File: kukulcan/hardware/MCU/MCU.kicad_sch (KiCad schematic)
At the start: 84 parts, among them J1 Barrel_Jack_5V_In, J2 Barrel_Jack_5V_In, J3 MiniPCIe Socket, J4 USB_C_Receptacle, J5 SMA_GNSS, Q1 AO3401A, U1 NEO-M8N, U2 ESP32-S3R16V, U3 W25Q256JWEIQ, U4 TLV1117-33, U5 BMI088, U6 BME280, U8 BNO055, X1 40MHz, Y1 32.768kHz

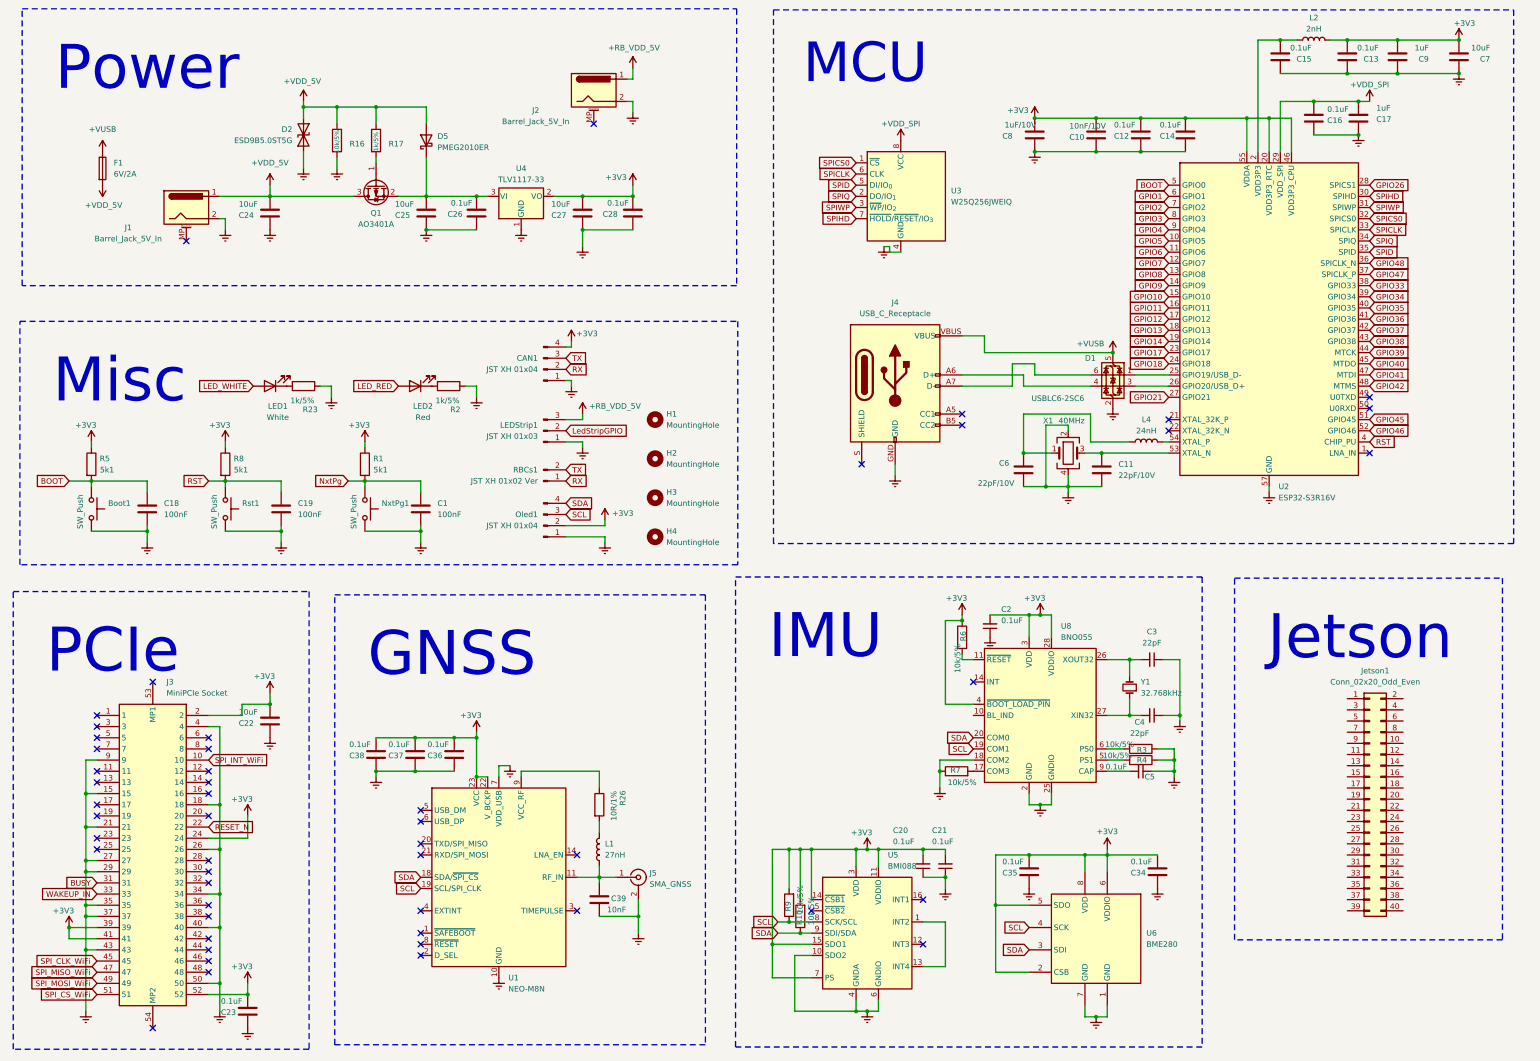
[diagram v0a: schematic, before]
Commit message: feat(kukulcan): several layout and schematic improvements, tasks pending. PCIe connector out.
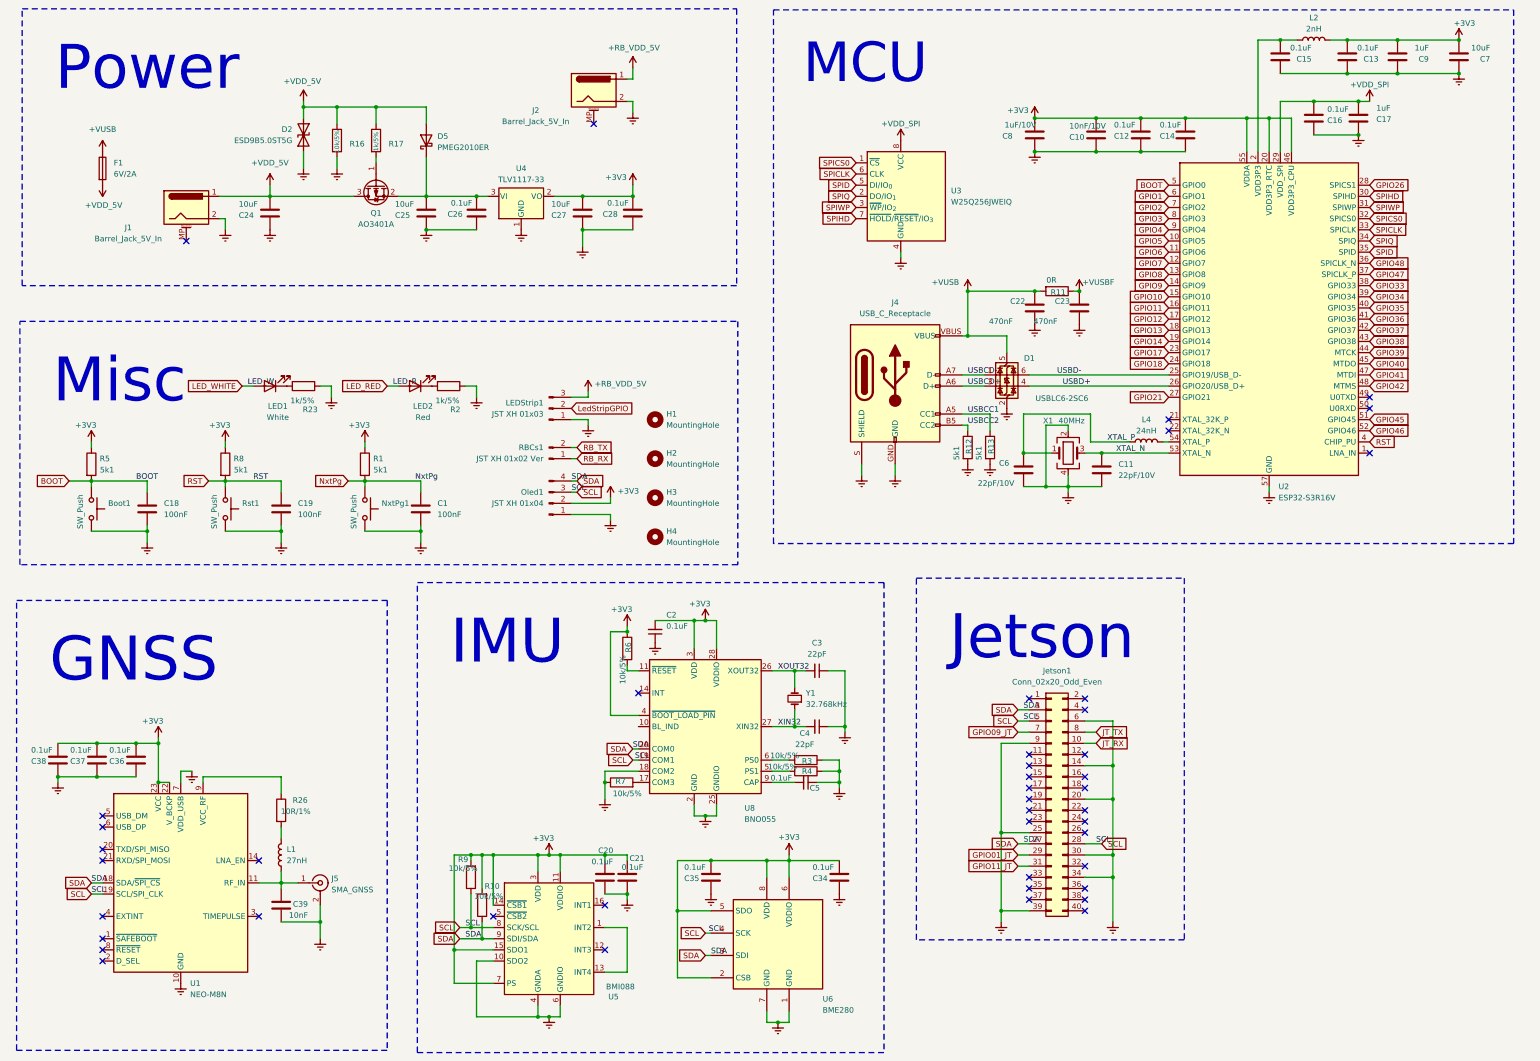
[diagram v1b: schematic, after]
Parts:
- removed C20, C21: 0.1uF, Capacitor_SMD:C_0402_1005Metric_Pad0.74x0.62mm_HandSolder, symbol PCM_SparkFun-Capacitor:C
- removed CAN1: JST XH 01x04, Connector_JST:JST_XH_S4B-XH-SM4-TB_1x04-1MP_P2.50mm_Horizontal, symbol Connector:Conn_01x04_Pin
- removed J3: MiniPCIe Socket, Core_System_2026:MiniPCIeSocket, symbol PCIeSocket:2041119-1
- added C20, C21: 0.1uF, Capacitor_SMD:C_0402_1005Metric_Pad0.74x0.62mm_HandSolder, symbol Device:C
- added R11: 0R, Resistor_SMD:R_0402_1005Metric_Pad0.72x0.64mm_HandSolder, symbol Device:R
- added R12, R13: 5k1, Resistor_SMD:R_0402_1005Metric_Pad0.72x0.64mm_HandSolder, symbol Device:R
- C22: value 10uF -> 470nF
- C23: value 0.1uF -> 470nF
- C24, C25, C27, C7: footprint Capacitor_SMD:C_0402_1005Metric_Pad0.74x0.62mm_HandSolder -> Capacitor_SMD:C_0805_2012Metric_Pad1.18x1.45mm_HandSolder
- F1: footprint Fuse:Fuse_0402_1005Metric_Pad0.77x0.64mm_HandSolder -> Fuse:Fuse_0805_2012Metric
- J4: footprint PCM_SparkFun-Connector:USB-C_16 -> Connector_USB:USB_C_Receptacle_GCT_USB4105-xx-A_16P_TopMnt_Horizontal
- LEDStrip1: footprint Connector_JST:JST_XH_S3B-XH-SM4-TB_1x03-1MP_P2.50mm_Horizontal -> Connector_JST:JST_XH_B3B-XH-A_1x03_P2.50mm_Vertical
- Oled1: footprint Connector_JST:JST_XH_S4B-XH-SM4-TB_1x04-1MP_P2.50mm_Horizontal -> Connector_JST:JST_XH_B4B-XH-A_1x04_P2.50mm_Vertical
- RBCs1: footprint Connector_JST:JST_XH_S2B-XH-A_1x02_P2.50mm_Horizontal -> Connector_JST:JST_XH_B2B-XH-A_1x02_P2.50mm_Vertical
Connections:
- net +3V3: now also C20.1, C21.1; no longer C22.1, C23.1
- net +VUSB: now also C22.2, R11.2
- net GND: now also C22.1, C23.1, J4.S (SHIELD), Jetson1.14 (Pin_14), Jetson1.20 (Pin_20), Jetson1.25 (Pin_25), Jetson1.30 (Pin_30), Jetson1.34 (Pin_34), Jetson1.39 (Pin_39), Jetson1.6 (Pin_6), Jetson1.9 (Pin_9), C20.2, C21.2, R12.2, R13.2; no longer C22.2, C23.2
- net SCL: now also Jetson1.28 (Pin_28), Jetson1.5 (Pin_5)
- net SDA: now also Jetson1.27 (Pin_27), Jetson1.3 (Pin_3)
- net USBCC1: now reaches J4.A5 (CC1)
- net USBCC1: now also R13.1
- net USBCD+: now reaches J4.A6 (D+), J4.B6 (D+)
- net USBCD+: now also D1.3 (I/O2); no longer D1.4 (I/O2)
- net USBCD-: now reaches J4.A7 (D-), J4.B7 (D-)
- net USBCD-: now also D1.1 (I/O1); no longer D1.6 (I/O1)
- net USBCC2: now reaches J4.B5 (CC2)
- net USBCC2: now also R12.1
- net USBD-: now reaches U2.25 (GPIO19/USB_D-)
- net USBD-: now also D1.6 (I/O1); no longer D1.1 (I/O1)
- net USBD+: now reaches U2.26 (GPIO20/USB_D+)
- net USBD+: now also D1.4 (I/O2); no longer D1.3 (I/O2)
- net XTAL_N: now reaches C11.1, U2.53 (XTAL_N), X1.3
- net XOUT32: now reaches C3.2, U8.26 (XOUT32), Y1.2
- net XIN32: now reaches C4.2, U8.27 (XIN32), Y1.1
- net JT_RX: now reaches Jetson1.10 (Pin_10)
- net GPIO01_JT: now reaches Jetson1.29 (Pin_29)
- net GPIO11_JT: now reaches Jetson1.31 (Pin_31)
- net GPIO09_JT: now reaches Jetson1.7 (Pin_7)
- net JT_TX: now reaches Jetson1.8 (Pin_8)
- net XTAL_P: now reaches C6.2, L4.1, X1.1
- net RX renamed RB_RX
- net TX renamed RB_TX
- new net +VUSBF: C23.2, R11.1
- no-connect marks 51 -> 44
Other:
- moved on the sheet: C2, C3, C34, C35, C36, C37, C38, C39, C4, C5, D1, J5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

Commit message: feat(kukulcan): current beta
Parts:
- removed C22, C23: 470nF, Capacitor_SMD:C_0402_1005Metric_Pad0.74x0.62mm_HandSolder, symbol Device:C
- added R12: 5k1, Resistor_SMD:R_0402_1005Metric_Pad0.72x0.64mm_HandSolder, symbol Device:R
- R11: value 0R -> 5k1
- renumbered C15 to C1, C14 to C10, C24 to C11, C25 to C12, C26 to C13, C27 to C14, C28 to C15, C6 to C16, C11 to C17, C13 to C2, C1 to C20, C2 to C21, C3 to C22, C4 to C23, C38 to C24, C37 to C25, C36 to C26, C5 to C27, C20 to C28, C21 to C29, C9 to C3, C35 to C30, C34 to C31, C39 to C32, C7 to C4, C16 to C5, C17 to C6, C8 to C7, C10 to C8, C12 to C9, D2 to D1, D5 to D2, D1 to D3, J2 to J1, J1 to J2, J4 to J3, J5 to J4, L2 to L1, L4 to L2, L1 to L3, R16 to R1, R6 to R10, R3 to R13, R4 to R14, R7 to R15, R26 to R16, R9 to R17, R10 to R18, R17 to R2, R23 to R3, R2 to R4, R12 to R5, R13 to R6, R5 to R7, R1 to R9, U4 to U1, U3 to U2, U2 to U3, U8 to U4, U1 to U5, U5 to U6, U6 to U7
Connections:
- net +VUSBF is gone; now on net +3V3: R11.1
- net GPIO33 is gone; now on net JTMCU1: U3.38 (GPIO33)
- net GPIO34 is gone; now on net NxtPg: U3.39 (GPIO34)
- net GPIO35 is gone; now on net JTMCU2: U3.40 (GPIO35)
- net GPIO36 is gone; now on net RST: U3.41 (GPIO36)
- net GPIO37 is gone; now on net JTMCU3: U3.42 (GPIO37)
- net GPIO38 is gone; now on net BOOT: U3.43 (GPIO38)
- net SCL is gone; now on net GND: Jetson1.28 (Pin_28), Jetson1.5 (Pin_5), Oled1.3 (Pin_3), R17.1, U4.19 (COM1), U5.19 (SCL/SPI_CLK), U6.8 (SCK/SCL), U7.4 (SCK)
- net SDA is gone; now on net GND: Jetson1.27 (Pin_27), Jetson1.3 (Pin_3), Oled1.4 (Pin_4), R18.1, U4.20 (COM0), U5.18 (SDA/~{SPI_CS}), U6.9 (SDI/SDA), U7.3 (SDI)
- net +3V3: now also R12.1
- net +VUSB: no longer R11.2
- net GND: now also R11.2, R12.2
- net XTAL_P: now also L2.2, U3.54 (XTAL_P); no longer C16.2, L2.1, X1.1
- net GPIO01_JT renamed JTMCU2
- net GPIO09_JT renamed JTMCU1
- net GPIO11_JT renamed JTMCU3
- net GPIO26: no longer names the net of U3.28 (SPICS1)
- net GPIO47: no longer names the net of U3.37 (SPICLK_P)
- net GPIO48: no longer names the net of U3.36 (SPICLK_N)
- new net: C16.2, L2.1, X1.1
- no-connect marks 44 -> 47
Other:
- moved on the sheet: L2

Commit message: feat(kukulcan): final schematic draft
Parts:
- removed H1, H2, H3, H4: MountingHole, MountingHole:MountingHole_3.2mm_M3_Pad_Via, symbol Mechanical:MountingHole
- added FID1, FID2, FID3, FID4, FID5, FID6: Fiducial, Fiducial:Fiducial_Cross_1.5mm_Mask2mm, symbol Mechanical:Fiducial
- added H1, H2, H3, H4: MountingHole_Pad, MountingHole:MountingHole_3.2mm_M3_Pad_TopBottom, symbol Mechanical:MountingHole_Pad
- C1, C10, C13, C15, C16, C17, C18, C19, C2, C20, C21, C22, C23, C24, C25, C26, C27, C28, C29, C3, C30, C31, C32, C5, C6, C7, C8, C9: footprint Capacitor_SMD:C_0402_1005Metric_Pad0.74x0.62mm_HandSolder -> Capacitor_SMD:C_0805_2012Metric_Pad1.18x1.45mm_HandSolder
- L1, L2, L3: footprint Inductor_SMD:L_0402_1005Metric_Pad0.77x0.64mm_HandSolder -> Inductor_SMD:L_0805_2012Metric_Pad1.05x1.20mm_HandSolder
- LED1, LED2: footprint LED_SMD:LED_1206_3216Metric_Pad1.42x1.75mm_HandSolder -> LED_SMD:LED_0805_2012Metric_Pad1.15x1.40mm_HandSolder
- R1, R10, R11, R12, R13, R14, R15, R16, R17, R18, R2, R3, R4, R5, R6, R7, R8, R9: footprint Resistor_SMD:R_0402_1005Metric_Pad0.72x0.64mm_HandSolder -> Resistor_SMD:R_0805_2012Metric_Pad1.20x1.40mm_HandSolder
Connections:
- net GPIO1 is gone; now on net NxtPg: U3.6 (GPIO1)
- net GPIO3 is gone; now on net JT_TX: U3.8 (GPIO3)
- net GPIO4 is gone; now on net JT_RX: U3.9 (GPIO4)
- net GPIO41 is gone; now on net RB_TX: U3.47 (MTDI)
- net GPIO42 is gone; now on net RB_RX: U3.48 (MTMS)
- net BOOT: no longer U3.43 (GPIO38)
- net GND: now also U4.10 (BL_IND), H1.1, H2.1, H3.1, H4.1; no longer Jetson1.27 (Pin_27), Jetson1.28 (Pin_28), Jetson1.3 (Pin_3), Jetson1.5 (Pin_5), Oled1.3 (Pin_3), Oled1.4 (Pin_4), R11.2, R12.2, R17.1, R18.1, U4.19 (COM1), U4.20 (COM0), U5.18 (SDA/~{SPI_CS}), U5.19 (SCL/SPI_CLK), U6.8 (SCK/SCL), U6.9 (SDI/SDA), U7.3 (SDI), U7.4 (SCK)
- net LED_RED: now also U3.41 (GPIO36)
- net LED_WHITE: now also U3.42 (GPIO37)
- net LedStripGPIO: now also U3.43 (GPIO38)
- net NxtPg: no longer U3.39 (GPIO34)
- net RST: no longer U3.41 (GPIO36)
- net GPIO10: no longer names the net of U3.15 (GPIO10)
- net GPIO11: no longer names the net of U3.16 (GPIO11)
- net GPIO12: no longer names the net of U3.17 (GPIO12)
- net GPIO13 renamed SDA
- net SDA: now also Jetson1.27 (Pin_27), Jetson1.3 (Pin_3), Oled1.4 (Pin_4), R11.2, R18.1, U4.20 (COM0), U5.18 (SDA/~{SPI_CS}), U6.9 (SDI/SDA), U7.3 (SDI)
- net GPIO14 renamed SCL
- net SCL: now also Jetson1.28 (Pin_28), Jetson1.5 (Pin_5), Oled1.3 (Pin_3), R12.2, R17.1, U4.19 (COM1), U5.19 (SCL/SPI_CLK), U6.8 (SCK/SCL), U7.4 (SCK)
- net GPIO17: no longer names the net of U3.23 (GPIO17)
- net GPIO18: no longer names the net of U3.24 (GPIO18)
- net GPIO2: no longer names the net of U3.7 (GPIO2)
- net GPIO21: no longer names the net of U3.27 (GPIO21)
- net GPIO39: no longer names the net of U3.44 (MTCK)
- net GPIO40: no longer names the net of U3.45 (MTDO)
- net GPIO45: no longer names the net of U3.51 (GPIO45)
- net GPIO46: no longer names the net of U3.52 (GPIO46)
- net GPIO5: no longer names the net of U3.10 (GPIO5)
- net GPIO6: no longer names the net of U3.11 (GPIO6)
- net GPIO7: no longer names the net of U3.12 (GPIO7)
- net GPIO8: no longer names the net of U3.13 (GPIO8)
- net GPIO9: no longer names the net of U3.14 (GPIO9)
- net JTMCU1 renamed JT_MCU1
- net JTMCU2 renamed JT_MCU2
- net JT_MCU2: now also U3.39 (GPIO34); no longer U3.40 (GPIO35)
- net JTMCU3 renamed JT_MCU3
- net JT_MCU3: now also U3.40 (GPIO35); no longer U3.42 (GPIO37)
- no-connect marks 47 -> 63
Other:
- moved on the sheet: Jetson1, LED1, LED2, LEDStrip1, Oled1, R3, R4, RBCs1

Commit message: feat(kukulcan): partial final PCB draft, GNSS pending
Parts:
- removed R11, R12: 5k1, Resistor_SMD:R_0805_2012Metric_Pad1.20x1.40mm_HandSolder, symbol Device:R
- C1, C10, C11, C12, C13, C14, C15, C16, C17, C18, C19, C2, C20, C21, C22, C23, C24, C25, C26, C27, C28, C29, C3, C30, C31, C32, C4, C5, C6, C7, C8, C9: footprint Capacitor_SMD:C_0805_2012Metric_Pad1.18x1.45mm_HandSolder -> Capacitor_SMD:C_0603_1608Metric_Pad1.08x0.95mm_HandSolder
- H1, H2, H3, H4: footprint MountingHole:MountingHole_3.2mm_M3_Pad_TopBottom -> MountingHole:MountingHole_3.2mm_M3_Pad_Via
- L1, L2, L3: footprint Inductor_SMD:L_0805_2012Metric_Pad1.05x1.20mm_HandSolder -> Inductor_SMD:L_0603_1608Metric_Pad1.05x0.95mm_HandSolder
- R1, R10, R2, R3, R4, R5, R6, R7, R8, R9: footprint Resistor_SMD:R_0805_2012Metric_Pad1.20x1.40mm_HandSolder -> Resistor_SMD:R_0603_1608Metric_Pad0.98x0.95mm_HandSolder
- R11: renamed from R13; footprint Resistor_SMD:R_0805_2012Metric_Pad1.20x1.40mm_HandSolder -> Resistor_SMD:R_0603_1608Metric_Pad0.98x0.95mm_HandSolder
- R12: renamed from R14; footprint Resistor_SMD:R_0805_2012Metric_Pad1.20x1.40mm_HandSolder -> Resistor_SMD:R_0603_1608Metric_Pad0.98x0.95mm_HandSolder
- R13: renamed from R15; footprint Resistor_SMD:R_0805_2012Metric_Pad1.20x1.40mm_HandSolder -> Resistor_SMD:R_0603_1608Metric_Pad0.98x0.95mm_HandSolder
- R14: renamed from R16; footprint Resistor_SMD:R_0805_2012Metric_Pad1.20x1.40mm_HandSolder -> Resistor_SMD:R_0603_1608Metric_Pad0.98x0.95mm_HandSolder
- R15: renamed from R17; footprint Resistor_SMD:R_0805_2012Metric_Pad1.20x1.40mm_HandSolder -> Resistor_SMD:R_0603_1608Metric_Pad0.98x0.95mm_HandSolder
- R16: renamed from R18; footprint Resistor_SMD:R_0805_2012Metric_Pad1.20x1.40mm_HandSolder -> Resistor_SMD:R_0603_1608Metric_Pad0.98x0.95mm_HandSolder
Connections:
- net JT_MCU1: now also Jetson1.29 (Pin_29), U3.11 (GPIO6); no longer Jetson1.7 (Pin_7), U3.38 (GPIO33)
- net JT_MCU2: now also Jetson1.31 (Pin_31), U3.9 (GPIO4); no longer Jetson1.29 (Pin_29), U3.39 (GPIO34)
- net JT_RX: now also U3.14 (GPIO9); no longer U3.9 (GPIO4)
- net JT_TX: now also U3.13 (GPIO8); no longer U3.8 (GPIO3)
- net LED_RED: now also U3.39 (GPIO34); no longer U3.41 (GPIO36)
- net LED_WHITE: now also U3.38 (GPIO33); no longer U3.42 (GPIO37)
- net RB_RX: now also U3.41 (GPIO36); no longer U3.48 (MTMS)
- net RB_TX: now also U3.40 (GPIO35); no longer U3.47 (MTDI)
- net SCL: now also U3.16 (GPIO11); no longer Jetson1.28 (Pin_28), U3.19 (GPIO14)
- net SDA: now also U3.15 (GPIO10); no longer Jetson1.27 (Pin_27), U3.18 (GPIO13)
- removed net JT_MCU3: Jetson1.31 (Pin_31), U3.40 (GPIO35)
- net LedStripGPIO: no longer names the net of U3.43 (GPIO38)
- net LedStripGPIO: no longer LEDStrip1.2 (Pin_2)
- new net LedStrip: LEDStrip1.2 (Pin_2), U3.42 (GPIO37)
- no-connect marks 63 -> 67

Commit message: hw(mcu): update schematic and pcb
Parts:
- Boot1, NxtPg1, Rst1: LCSC (none) -> C221930; Manufacturer (none) -> C&K; Manufacturer Part Number (none) -> RS-282G05A3-SMRT
- C1, C10, C13, C15, C18, C19, C2, C20, C21, C24, C25, C26, C27, C28, C29, C30, C31, C5, C9: LCSC (none) -> C14663; Manufacturer (none) -> YAGEO; Manufacturer Part Number (none) -> CC0603KRX7R9BB104
- C11, C12, C14, C4: LCSC (none) -> C19702; Manufacturer (none) -> Samsung Electro-Mechanics; Manufacturer Part Number (none) -> CL10A106KP8NNNC
- C16, C17, C22, C23: LCSC (none) -> C326840; Manufacturer (none) -> YAGEO; Manufacturer Part Number (none) -> CC0603FRNPO9BN220
- C3, C6: LCSC (none) -> C1592; Manufacturer (none) -> Samsung Electro-Mechanics; Manufacturer Part Number (none) -> CL10A105KO8NNNC
- C32, C8: LCSC (none) -> C2168725; Manufacturer (none) -> KEMET; Manufacturer Part Number (none) -> C0603C103K8RACTU
- C7: LCSC (none) -> C26413; Manufacturer (none) -> Samsung Electro-Mechanics; Manufacturer Part Number (none) -> CL10A105KP8NNNC
- D1: LCSC (none) -> C111566; Manufacturer (none) -> onsemi; Manufacturer Part Number (none) -> ESD9B5.0ST5G
- D2: LCSC (none) -> C6952604; Manufacturer (none) -> Nexperia; Manufacturer Part Number (none) -> PMEG2010ER-QX
- D3: LCSC (none) -> C2827654; Manufacturer (none) -> TECH PUBLIC; Manufacturer Part Number (none) -> USBLC6-2SC6
- F1: LCSC (none) -> C70158; Manufacturer (none) -> TECHFUSE; Manufacturer Part Number (none) -> SL0805200
- FID1, FID2, FID3, FID4, FID5, FID6: footprint Fiducial:Fiducial_Cross_1.5mm_Mask2mm -> Fiducial:Fiducial_1mm_Mask3mm
- J1, J2: LCSC (none) -> C7498153; Manufacturer (none) -> Lian Xin Technology; Manufacturer Part Number (none) -> XDJK-0051-025
- J3: LCSC (none) -> C3020560; Manufacturer (none) -> Global Connector Technology; Manufacturer Part Number (none) -> USB4105-GF-A
- J4: footprint Connector_Coaxial:U.FL_Molex_MCRF_73412-0110_Vertical -> Connector_Coaxial:SMA_Amphenol_132134-10_Vertical; LCSC (none) -> C3172499; Manufacturer (none) -> Amphenol; Manufacturer Part Number (none) -> 132134-10
- Jetson1: LCSC (none) -> C2884029; Manufacturer (none) -> XKB Connection; Manufacturer Part Number (none) -> X6521WVS-2x20H-C60D74
- L1: LCSC (none) -> C395081; Manufacturer (none) -> FH; Manufacturer Part Number (none) -> VHF160808H2N0ST
- L2: LCSC (none) -> C139271; Manufacturer (none) -> FH; Manufacturer Part Number (none) -> VHF160808H24NJT
- L3: LCSC (none) -> C148128; Manufacturer (none) -> muRata; Manufacturer Part Number (none) -> LQW18AN27NG00D
- LED1: LCSC (none) -> C25170729; Manufacturer (none) -> YONGYUTAI; Manufacturer Part Number (none) -> YLED0805W
- LED2: LCSC (none) -> C19171391; Manufacturer (none) -> YONGYUTAI; Manufacturer Part Number (none) -> YLED0805R
- LEDStrip1: LCSC (none) -> C144394; Manufacturer (none) -> JST; Manufacturer Part Number (none) -> B3B-XH-A(LF)(SN)
- Oled1: LCSC (none) -> C144395; Manufacturer (none) -> JST; Manufacturer Part Number (none) -> B4B-XH-A(LF)(SN)
- Q1: LCSC (none) -> C15127; Manufacturer (none) -> AOS; Manufacturer Part Number (none) -> AO3401A
- R1, R10, R11, R12, R13, R15, R16: LCSC (none) -> C2889392; Manufacturer (none) -> VO; Manufacturer Part Number (none) -> 0603 ±5% 10K
- R14: LCSC (none) -> C22859; Manufacturer (none) -> UNI-ROYAL; Manufacturer Part Number (none) -> 0603WAF100JT5E
- R2, R3, R4: LCSC (none) -> C25585; Manufacturer (none) -> UNI-ROYAL; Manufacturer Part Number (none) -> 0603WAJ0102T5E
- R5, R6, R7, R8, R9: LCSC (none) -> C23186; Manufacturer (none) -> UNI-ROYAL; Manufacturer Part Number (none) -> 0603WAF5101T5E
- RBCs1: LCSC (none) -> C158012; Manufacturer (none) -> JST; Manufacturer Part Number (none) -> B2B-XH-A(LF)(SN)
- U1: LCSC (none) -> C37359; Manufacturer (none) -> TI; Manufacturer Part Number (none) -> TLV1117-33IDCYR
- U2: value W25Q256JWEIQ -> W25Q256JVEIQ; footprint Core_System_2026:W25Q256JWEIQ -> Core_System_2026:W25Q256JVEIQ; LCSC (none) -> C97522; Manufacturer (none) -> Winbond; Manufacturer Part Number (none) -> W25Q256JVEIQ
- U3: value ESP32-S3R16V -> ESP32-S3R8; footprint Core_System_2026:ESP32-S3R16V -> Core_System_2026:ESP32-S3R8; LCSC (none) -> C2913194; Manufacturer (none) -> ESPRESSIF; Manufacturer Part Number (none) -> ESP32-S3R8
- U4: LCSC (none) -> C93216; Manufacturer (none) -> Bosch; Manufacturer Part Number (none) -> BNO055
- U5: LCSC (none) -> C6330769; Manufacturer (none) -> U-BLOX; Manufacturer Part Number (none) -> NEO-M8N-0
- U6: LCSC (none) -> C194919; Manufacturer (none) -> Bosch; Manufacturer Part Number (none) -> BMI088
- U7: LCSC (none) -> C92489; Manufacturer (none) -> Bosch; Manufacturer Part Number (none) -> BME280
- X1: LCSC (none) -> C5265852; Manufacturer (none) -> Huiyuan crystal; Manufacturer Part Number (none) -> HY40MSMD2520GA1R30
- Y1: LCSC (none) -> C97606; Manufacturer (none) -> Seiko; Manufacturer Part Number (none) -> SC-32S32.768kHz20PPM12.5pF
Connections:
- net +VDD_SPI is gone; now on net +3V3: C5.1, C6.1, U2.8 (VCC), U3.29 (VDD_SPI)
- net RF2: now reaches L3.1, R14.2
- net RF_IN: now reaches C32.2, J4.1 (In), L3.2, U5.11 (RF_IN)
- net RF1: now reaches R14.1, U5.9 (VCC_RF)
